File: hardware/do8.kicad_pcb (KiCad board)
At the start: 4 copper layers, 100 x 85 mm, 116 parts, among them J101 TNG-Power-TOP, J102 TNG-Power-BTM, J103 TNG-Data-TOP, J104 TNG-Data-BTM, P102 Debug, P103 PE, P201 OUTPUT0, P202 OUTPUT1, P203 OUTPUT2, P204 OUTPUT3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

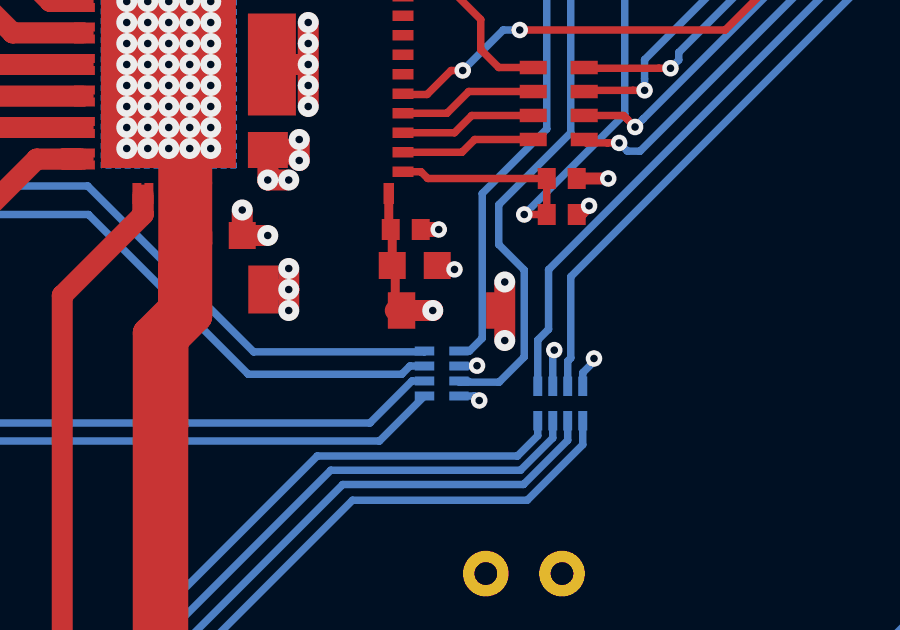
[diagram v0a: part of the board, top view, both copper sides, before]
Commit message: all footprints updated
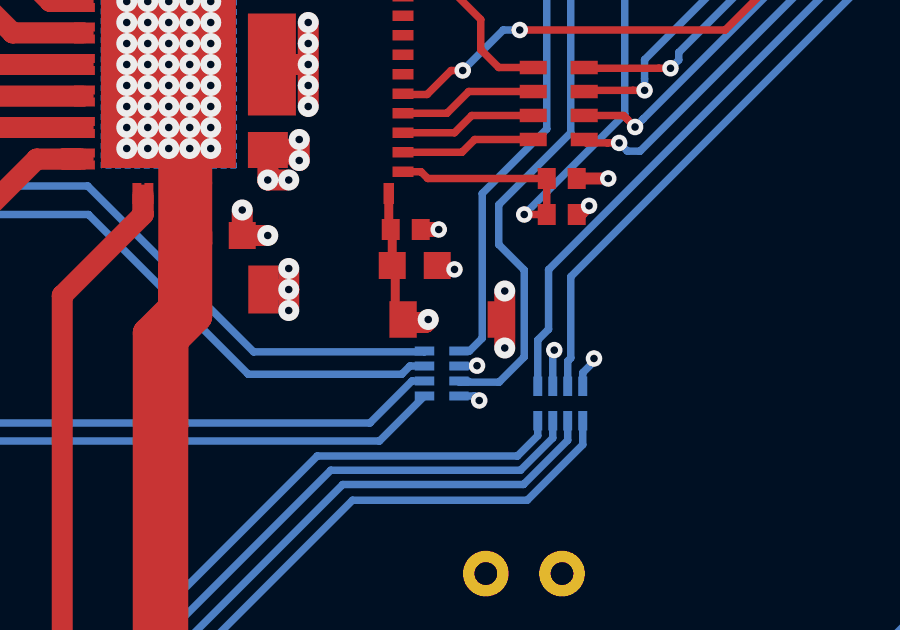
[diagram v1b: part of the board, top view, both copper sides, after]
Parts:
- C101, C102, C103, C104, C105, C106, C107, C108, C109, C112, C113, C114, C116, C117, C212, C214: footprint C0402F -> kicad-libraries:C0402F
- C115: footprint C0603F -> kicad-libraries:C0603F
- C118, C119, C120, C121, C125, C126, C127, C128: footprint C1206 -> kicad-libraries:C1206
- D210, D211, D212, D213, D214, D215, D216, D217: footprint LED-LP -> kicad-libraries:LED-LP
- J101, J103: footprint TNG-40-TOP -> kicad-libraries:TNG-40-TOP
- J102, J104: footprint TNG-40-BTM -> kicad-libraries:TNG-40-BTM
- L101, L102, L103, L104: footprint R0603F -> kicad-libraries:R0603F
- L105: footprint WE-CNSW-0603 -> kicad-libraries:WE-CNSW-0603
- LED101: footprint LED-RGB-LP -> kicad-libraries:LED-RGB-LP
- P201, P202, P203, P204: footprint OQ_4P -> kicad-libraries:OQ_4P
- R101, R102, R103, R104, R105, R106, R107, R108: footprint R0402F -> kicad-libraries:R0402F
- U103: footprint SOT563-SPEC -> kicad-libraries:SOT563-SPEC
- moved D209 0.30 mm to (123.2, 121.7)

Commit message: remove galvanic isolation as default
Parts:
- C101, C102, C103, C104, C105, C106, C107, C108, C109, C112, C113, C114, C116, C117, C212, C214: footprint kicad-libraries:C0402F -> C0402F
- C115: footprint kicad-libraries:C0603F -> C0603F
- C118, C121, C125, C126, C127, C128: footprint kicad-libraries:C1206 -> C1206
- C119, C120: value 1nF 2kV -> 0; footprint kicad-libraries:C1206 -> C1206
- D210, D211, D212, D213, D214, D215, D216, D217: footprint kicad-libraries:LED-LP -> LED-LP
- J101, J103: footprint kicad-libraries:TNG-40-TOP -> TNG-40-TOP
- J102, J104: footprint kicad-libraries:TNG-40-BTM -> TNG-40-BTM
- L101, L102, L103, L104: footprint kicad-libraries:R0603F -> R0603F
- L105: footprint kicad-libraries:WE-CNSW-0603 -> WE-CNSW-0603
- LED101: footprint kicad-libraries:LED-RGB-LP -> LED-RGB-LP
- P201, P202, P203, P204: footprint kicad-libraries:OQ_4P -> OQ_4P
- R101, R102, R103, R104, R105, R106, R107, R108: footprint kicad-libraries:R0402F -> R0402F
- U103: footprint kicad-libraries:SOT563-SPEC -> SOT563-SPEC
- U104: value TEL10 -> DNP

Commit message: fix 3d stuff
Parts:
- C101, C102, C103, C104, C105, C106, C107, C108, C109, C112, C113, C114, C116, C117, C212, C214: footprint C0402F -> kicad-libraries:C0402F
- C115: footprint C0603F -> kicad-libraries:C0603F
- C118, C119, C120, C121, C125, C126, C127, C128: footprint C1206 -> kicad-libraries:C1206
- D210, D211, D212, D213, D214, D215, D216, D217: footprint LED-LP -> kicad-libraries:LED-LP
- J101, J103: footprint TNG-40-TOP -> kicad-libraries:TNG-40-TOP
- J102, J104: footprint TNG-40-BTM -> kicad-libraries:TNG-40-BTM
- L101, L102, L103, L104: footprint R0603F -> kicad-libraries:R0603F
- L105: footprint WE-CNSW-0603 -> kicad-libraries:WE-CNSW-0603
- LED101: footprint LED-RGB-LP -> kicad-libraries:LED-RGB-LP
- P201, P202, P203, P204: footprint OQ_4P -> kicad-libraries:OQ_4P
- R101, R102, R103, R104, R105, R106, R107, R108: footprint R0402F -> kicad-libraries:R0402F
- U103: footprint SOT563-SPEC -> kicad-libraries:SOT563-SPEC
